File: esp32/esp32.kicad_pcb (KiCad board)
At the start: 2 copper layers, 80.5 x 93.5 mm, 54 parts, among them IC1 KF33BDT-TR, J1 USB_C, Q1 FDS9926A, Q2 FDN306P, Q3 BC817, Q4 BC817, SW1 ON-OFF, SW2 Reset, SW3 Boot, U1 AP5056, U2 DW01A, U3 CP2102, U4 ESP32-WROOM-32

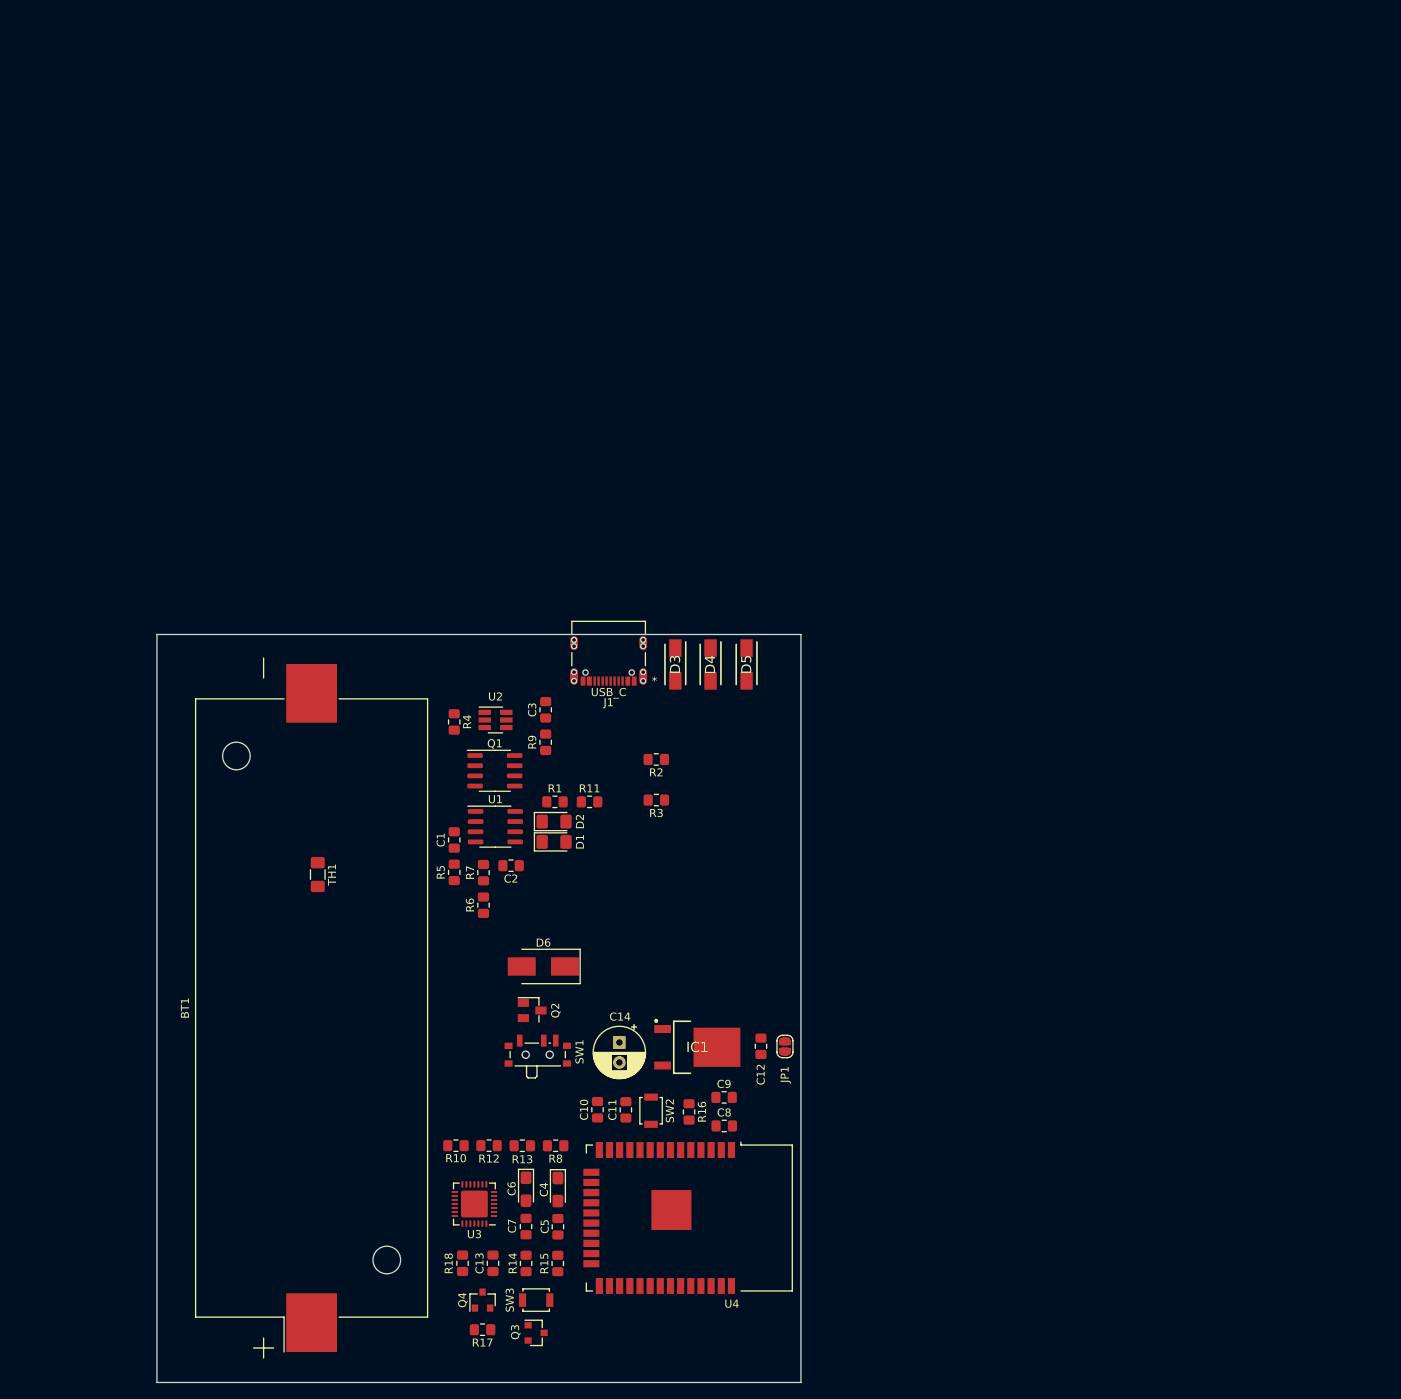
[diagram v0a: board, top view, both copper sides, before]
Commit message: Add PCB routing
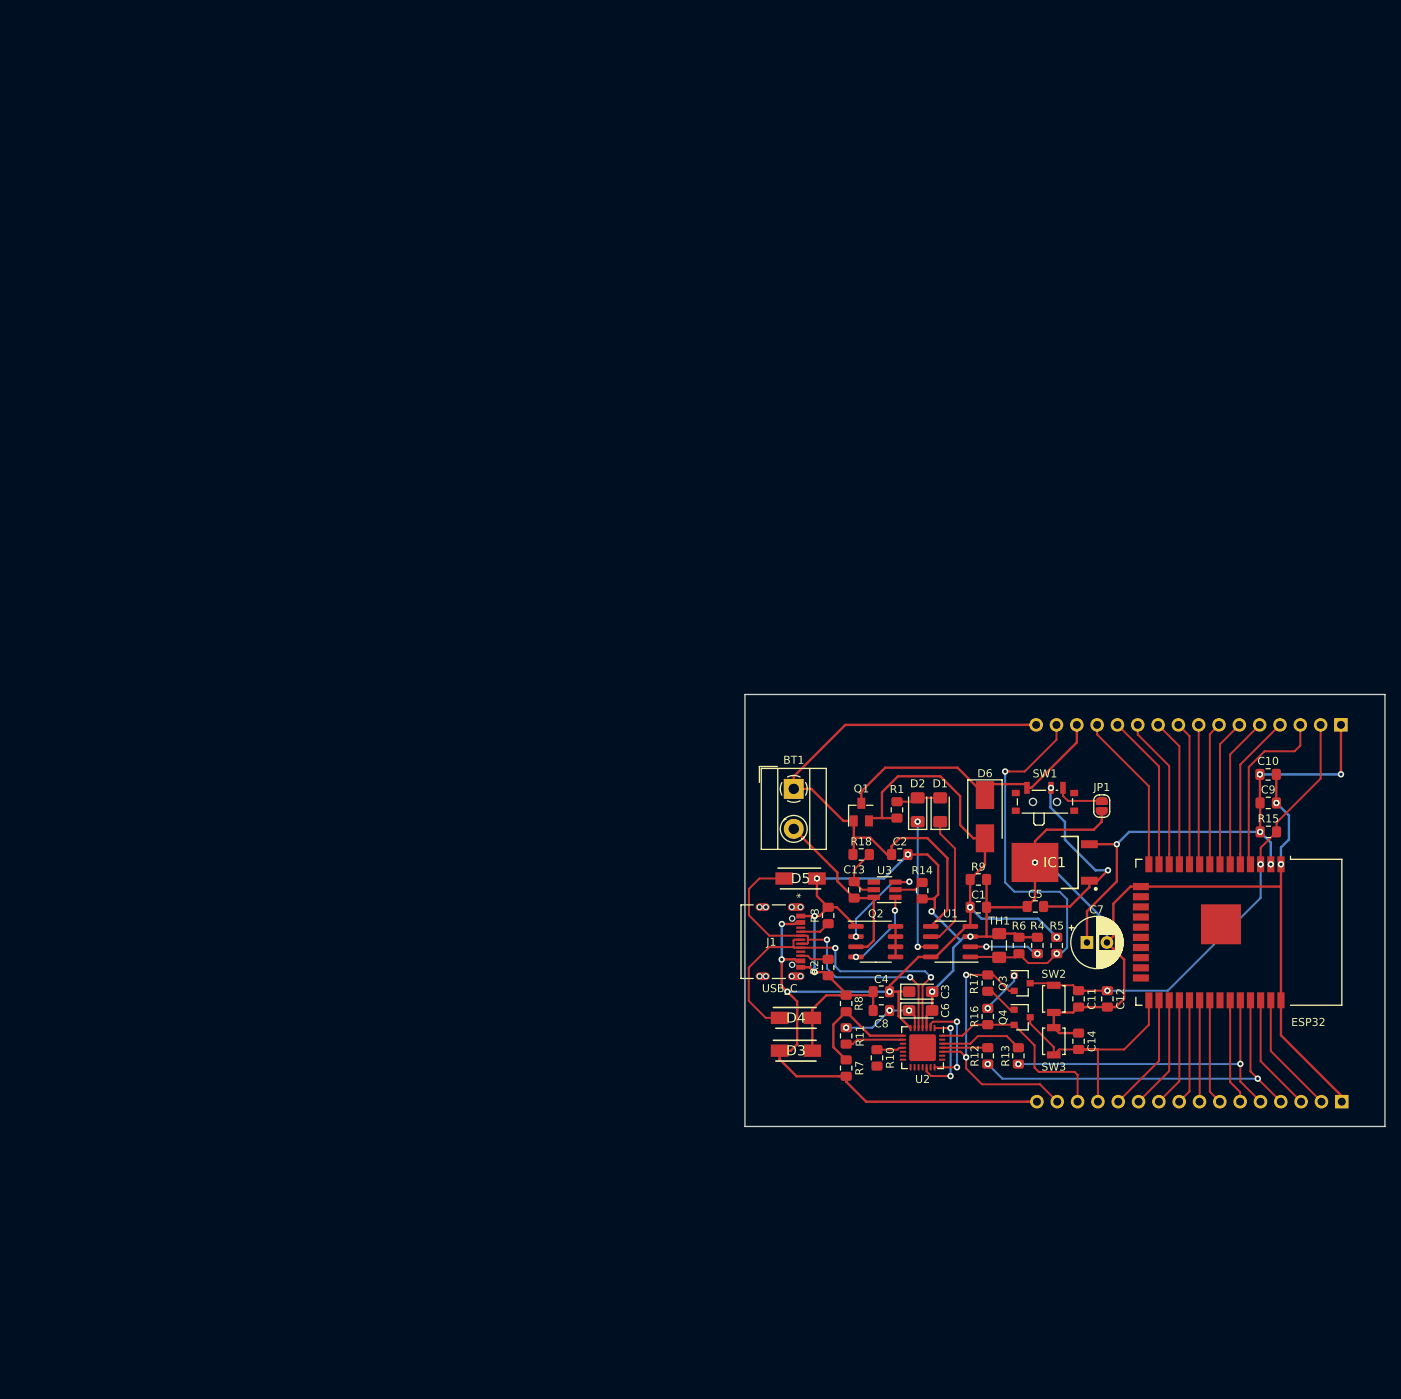
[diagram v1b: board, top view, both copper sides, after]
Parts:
- removed the C12 at (93.0, 128.0)
- removed the C7 at (63.6, 150.5)
- removed the Q1 at (59.7, 93.5)
- removed the R16 at (84.0, 136.2)
- removed the R9 at (66.1, 90.0)
- removed U4: ESP32-WROOM-32, RF_Module:ESP32-WROOM-32
- added C11: 1uF, Capacitor_SMD:C_0805_2012Metric_Pad1.15x1.40mm_HandSolder, F.Cu at (132.7, 122.0)
- added C14: 0.1uF, Capacitor_SMD:C_0805_2012Metric_Pad1.15x1.40mm_HandSolder, F.Cu at (132.7, 127.3)
- added ESP32: ESP32-WROOM-32, RF_Module:ESP32-WROOM-32, F.Cu at (149.7, 113.7)
- added J2: Conn_01x16, Connector_PinHeader_2.54mm:PinHeader_1x16_P2.54mm_Vertical, B.Cu at (165.5, 87.8)
- added J3: Conn_01x16, Connector_PinHeader_2.54mm:PinHeader_1x16_P2.54mm_Vertical, B.Cu at (165.6, 134.9)
- added Q2: FDS9926A, Package_SO:SOIC-8_3.9x4.9mm_P1.27mm, F.Cu at (107.3, 114.9)
- added R11: 4.7k, Resistor_SMD:R_0805_2012Metric_Pad1.15x1.40mm_HandSolder, F.Cu at (103.7, 126.7)
- added R17: 10k, Resistor_SMD:R_0805_2012Metric_Pad1.15x1.40mm_HandSolder, F.Cu at (121.3, 120.1)
- BT1: footprint BatteryHolder:BatteryHolder_SMT_1x26650 -> TerminalBlock_MetzConnect:TerminalBlock_MetzConnect_Type055_RT01502HDWU_1x02_P5.00mm_Horizontal
- C10: value 1uF -> 10uF
- C3: value 0.1uF -> 4.7uF; footprint Capacitor_SMD:C_0805_2012Metric_Pad1.15x1.40mm_HandSolder -> Capacitor_Tantalum_SMD:CP_EIA-3216-12_Kemet-S_Pad1.58x1.35mm_HandSolder
- C4: value 4.7uF -> 0.1uF; footprint Capacitor_Tantalum_SMD:CP_EIA-3216-12_Kemet-S_Pad1.58x1.35mm_HandSolder -> Capacitor_SMD:C_0805_2012Metric_Pad1.15x1.40mm_HandSolder
- C5: value 0.1uF -> 1uF
- C9: value 10uF -> 0.1uF
- R10: value 47.5k -> 10k
- R12, R18: value 10k -> 100
- R13: value 4.7k -> 100
- R14: value 100 -> 1k
- R15: value 100 -> 10k
- R5: value 1k -> RT1
- R6: value RT1 -> RT2
- R7: value RT2 -> 22.1k
- R8: value 22.1k -> 47.5k
- U2: value DW01A -> CP2102; footprint Package_TO_SOT_SMD:SOT-23-6_Handsoldering -> Package_DFN_QFN:QFN-28-1EP_5x5mm_P0.5mm_EP3.35x3.35mm
- U3: value CP2102 -> DW01A; footprint Package_DFN_QFN:QFN-28-1EP_5x5mm_P0.5mm_EP3.35x3.35mm -> Package_TO_SOT_SMD:SOT-23-6_Handsoldering
- moved R15 103.9 mm to (156.4, 101.2), turned to 0 degrees
- moved C10 93.7 mm to (156.4, 94.0), turned to 0 degrees
- moved TH1 85.6 mm to (122.8, 115.4), turned to 90 degrees
- moved R4 78.1 mm to (127.5, 115.4), turned to 90 degrees
- moved C9 77.3 mm to (156.4, 97.6)
- moved Q4 76.2 mm to (125.7, 124.3), turned to 0 degrees
- moved R5 75.9 mm to (130.0, 115.4), turned to 270 degrees
- moved Q3 74.8 mm to (125.7, 120.1)
- moved R16 74.3 mm to (121.3, 124.2), turned to 270 degrees
- moved SW3 72.3 mm to (129.6, 127.3), turned to 90 degrees
- moved C5 71.9 mm to (127.3, 110.5), turned to 180 degrees
- moved R18 71.4 mm to (105.5, 104.0), turned to 0 degrees
- moved SW1 70.8 mm to (128.5, 97.1)
- moved R14 68.0 mm to (113.2, 108.5), turned to 270 degrees
- moved U2 67.3 mm to (113.2, 128.2), turned to 270 degrees
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- renumbered C11 to C12, C14 to C7, Q2 to Q1, R17 to R16, R11 to R9
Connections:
- C10 pad 1: EN -> +3V3
- C13 pad 1: Boot -> Net-(C13-Pad1)
- C13 pad 2: Batt- -> Net-(BT1-Pad2)
- C3 pad 1: Net-(C3-Pad1) -> VBUS
- C3 pad 2: Net-(BT1-Pad2) -> Batt-
- C5 pad 1: VBUS -> Net-(C5-Pad1)
- C8 pad 1: +3V3 -> Net-(C6-Pad1)
- IC1 pad 1: Net-(C12-Pad1) -> Net-(C5-Pad1)
- R12 pad 1: Net-(R12-Pad1) -> Tx
- R12 pad 2: Batt- -> Net-(R12-Pad2)
- R13 pad 1: Net-(R13-Pad1) -> Rx
- R13 pad 2: Net-(C6-Pad1) -> Net-(R13-Pad2)
- R14 pad 2: Net-(R14-Pad2) -> Batt-
- R15 pad 1: Net-(R15-Pad1) -> +3V3
- R15 pad 2: Net-(R15-Pad2) -> EN
- R18 pad 1: Net-(Q4-Pad1) -> Batt+
- R18 pad 2: RTS -> Net-(C13-Pad1)
- R5 pad 1: Net-(R5-Pad1) -> VBUS
- R5 pad 2: Batt- -> Temp
- R6 pad 1: VBUS -> Temp
- R6 pad 2: Net-(R6-Pad2) -> Batt-
- R7 pad 1: Net-(R6-Pad2) -> VBUS
- R7 pad 2: Batt- -> Net-(R7-Pad2)
- R8 pad 1: VBUS -> Net-(R7-Pad2)
- R8 pad 2: Net-(R10-Pad1) -> Batt-
- SW1 pad 2: Net-(C12-Pad1) -> Net-(C5-Pad1)
- TH1 pad 1: Net-(R6-Pad2) -> Temp
- U1 pad 1: Net-(R6-Pad2) -> Temp
- U1 pad 2: Net-(R5-Pad1) -> Net-(R4-Pad1)
- U2 pad 1: Net-(Q1-Pad4) -> Net-(U2-Pad1)
- U2 pad 2: Net-(R4-Pad1) -> Net-(U2-Pad2)
- U2 pad 3: Net-(Q1-Pad2) -> Batt-
- U2 pad 4: Net-(U2-Pad4) -> Net-(D4-Pad1)
- U2 pad 5: Net-(C3-Pad1) -> Net-(D5-Pad1)
- U2 pad 6: Net-(BT1-Pad2) -> Net-(C6-Pad1)
- U3 pad 1: Net-(U3-Pad1) -> Net-(Q2-Pad4)
- U3 pad 2: Net-(U3-Pad2) -> Net-(R14-Pad1)
- U3 pad 3: Batt- -> Net-(Q2-Pad2)
- U3 pad 4: Net-(D4-Pad1) -> Net-(U3-Pad4)
- U3 pad 5: Net-(D5-Pad1) -> Net-(C13-Pad1)
- U3 pad 6: Net-(C6-Pad1) -> Net-(BT1-Pad2)
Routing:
- net Batt-: track 0.00 -> 236.6 mm, vias 0 -> 10
- net VBUS: track 0.00 -> 143.5 mm, vias 0 -> 6
- net Batt+: track 0.00 -> 72.4 mm
- net +3V3: track 0.00 -> 63.9 mm, vias 0 -> 5
- net EN: track 0.00 -> 58.7 mm, vias 0 -> 2
- net Temp: track 0.00 -> 52.0 mm, vias 0 -> 2
- net Tx: track 0.00 -> 48.8 mm, vias 0 -> 2
- net Net-(D4-Pad1): track 0.00 -> 44.2 mm, vias 0 -> 2
- net Net-(D5-Pad1): track 0.00 -> 42.1 mm, vias 0 -> 2
- net Rx: track 0.00 -> 41.5 mm, vias 0 -> 2
- net Vin: track 0.00 -> 37.2 mm
- net RTS: track 0.00 -> 34.9 mm, vias 0 -> 2
- net Boot: track 0.00 -> 31.4 mm
- net DTR: track 0.00 -> 25.1 mm
- net Net-(C5-Pad1): track 0.00 -> 24.6 mm, vias 0 -> 2
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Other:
- board size 80.5 x 93.5 mm -> 80 x 54 mm
- net class PWR added: clearance 0.2, trace_width 0.3, via_dia 0.8, via_drill 0.4

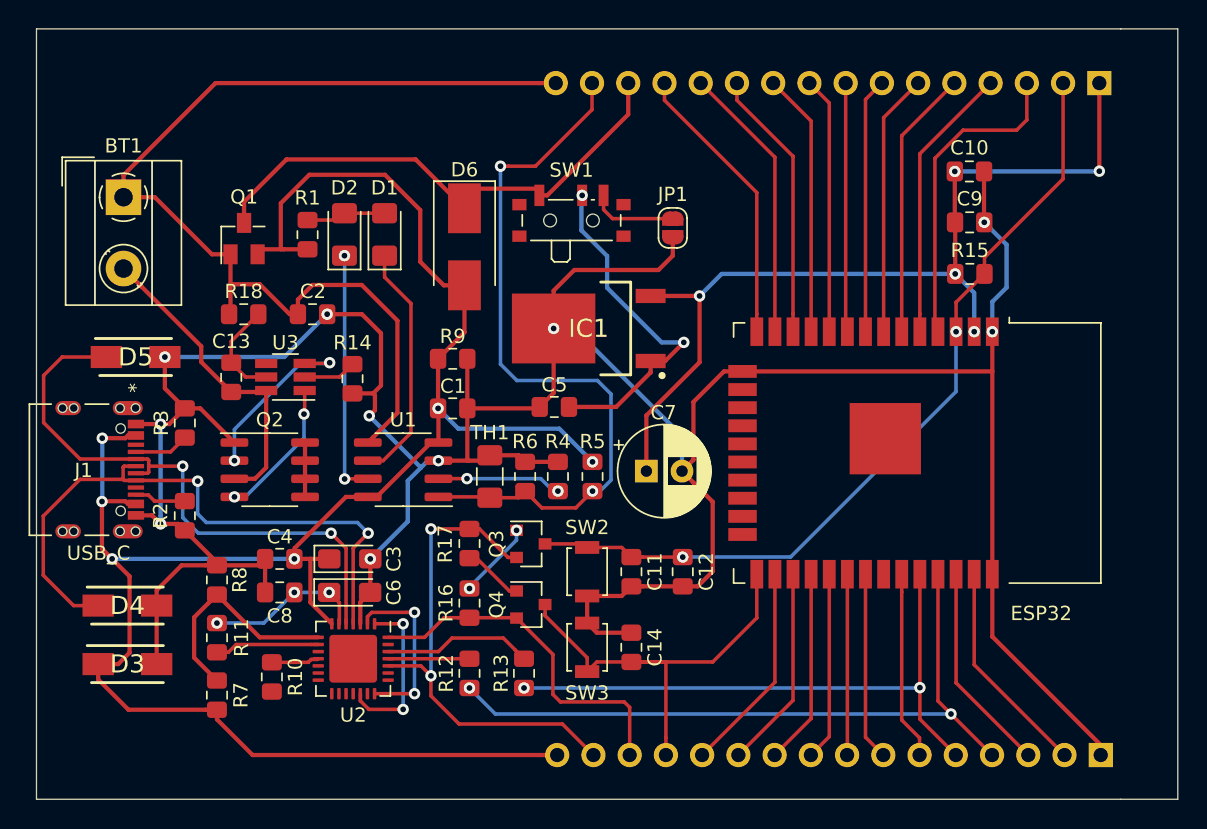
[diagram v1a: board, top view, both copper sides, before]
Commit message: 1) Power tracks to 30 milis - 2) Add more pins for symmetry
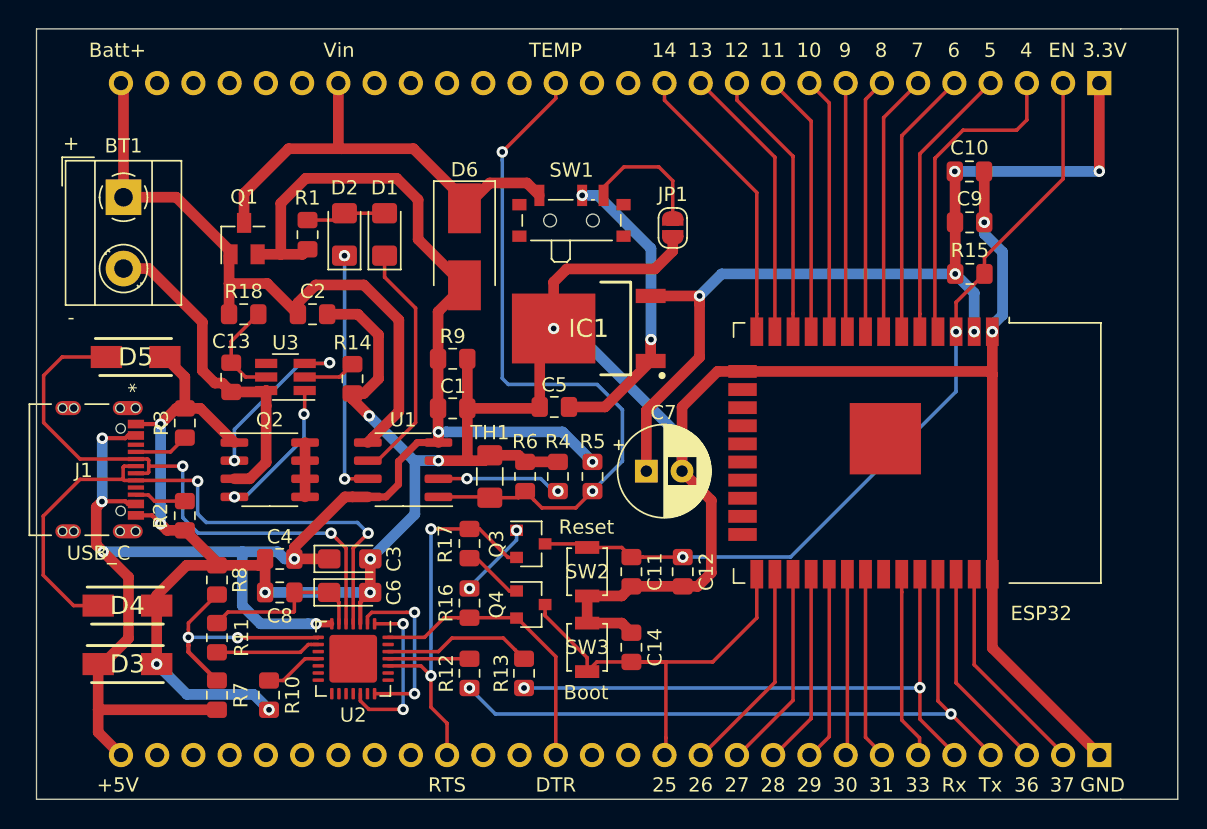
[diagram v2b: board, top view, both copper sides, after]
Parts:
- removed J2, J3: Conn_01x16, Connector_PinHeader_2.54mm:PinHeader_1x16_P2.54mm_Vertical
- added J4: Conn_01x28, Connector_PinHeader_2.54mm:PinHeader_1x28_P2.54mm_Vertical, B.Cu at (165.5, 87.8)
- added J5: Conn_01x28, Connector_PinHeader_2.54mm:PinHeader_1x28_P2.54mm_Vertical, B.Cu at (165.5, 134.9)
- moved R10 1.29 mm to (107.3, 130.7)
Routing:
- net Batt-: track 236.6 -> 264.2 mm, vias 10 -> 12
- net Batt+: track 72.4 -> 50.5 mm
- net VBUS: track 143.5 -> 131.2 mm, vias 6 -> 7
- net RTS: track 34.9 -> 26.4 mm
- net Vin: track 37.2 -> 31.9 mm
- net DTR: track 25.1 -> 20.3 mm
- net Net-(C5-Pad1): track 24.6 -> 21.3 mm
- net Net-(JP1-Pad1): track 6.11 -> 9.06 mm
- net Temp: track 52.0 -> 50.1 mm
- net Net-(BT1-Pad2): track 22.2 -> 23.4 mm
- net Net-(R7-Pad2): track 15.7 -> 16.8 mm, vias 0 -> 2
- net Net-(C6-Pad1): track 11.3 -> 12.0 mm, vias 3 -> 0
- net Net-(R10-Pad1): track 3.35 -> 4.08 mm
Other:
- net class PWR: trace_width 0.3 -> 0.75
- board text added: "+"
- board text added: "+5V"
- board text added: "-"
- board text added: "10"
- board text added: "11"
- board text added: "12"
- board text added: "13"
- board text added: "14"
- board text added: "25"
- board text added: "26"
- board text added: "27"
- board text added: "28"
- board text added: "29"
- board text added: "3.3V"
- board text added: "30"
- board text added: "31"
- board text added: "33"
- board text added: "36"
- board text added: "37"
- board text added: "4"
- board text added: "5"
- board text added: "6"
- board text added: "7"
- board text added: "8"
- board text added: "9"
- board text added: "Batt+"
- board text added: "Boot"
- board text added: "DTR"
- board text added: "EN"
- board text added: "GND"
- board text added: "RTS"
- board text added: "Reset"
- board text added: "Rx"
- board text added: "TEMP"
- board text added: "Tx"
- board text added: "Vin"
